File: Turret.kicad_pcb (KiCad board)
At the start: 2 copper layers, 104 x 54 mm, 26 parts, among them J1 172298-1108, J2 501645-1620

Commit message: Cleaned up hiearchical labels and local labels
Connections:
- net /SWD_3V3 renamed /SWD_{3V3}
- net /SWD_GND renamed /SWD_{GND}
- net /SWD_SWCLK renamed /SWD_{SWCLK}
- net /SWD_SWDIO renamed /SWD_{SWDIO}

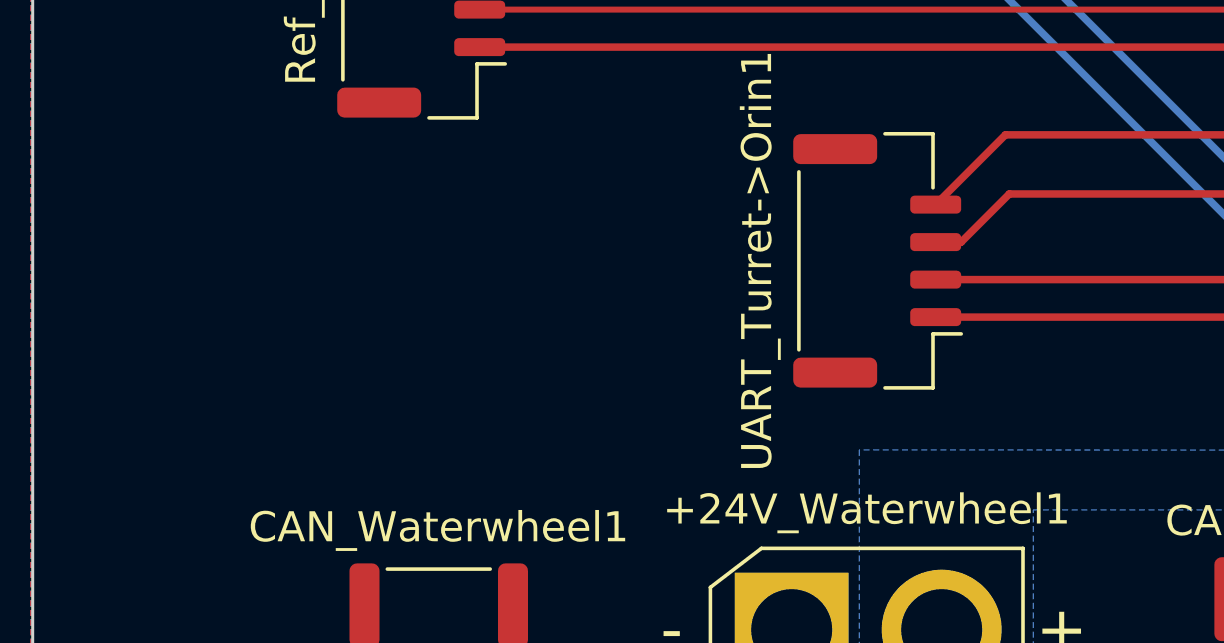
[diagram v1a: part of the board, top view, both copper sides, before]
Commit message: Added UV LED connection
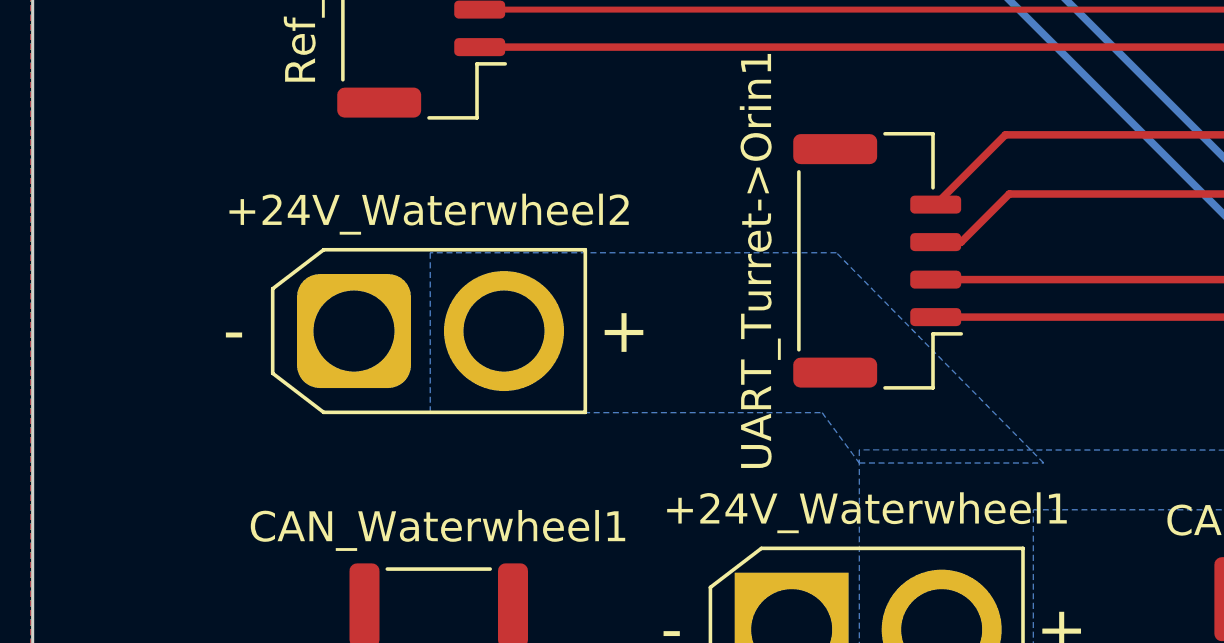
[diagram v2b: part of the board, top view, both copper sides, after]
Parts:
- added +24V_Waterwheel2: Conn_01x02_Pin, Connector_AMASS:AMASS_XT30U-F_1x02_P5.0mm_Vertical, F.Cu at (51.2, 69.0)
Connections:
- net /+19V renamed /OrinPWR_{+19V}
- net /+24V_Gimbal renamed /Gimbal_{+24V}
- net /+24V_Shooter renamed /Shooter_{+24V}
- net /CANGim_H renamed /CAN1+
- net /CANGim_L renamed /CAN1-
- net /CANH renamed /CAN2+
- net /CANL renamed /CAN2-
- net /Gimbal_PWR_GND renamed /Gimbal_{GND}
- net /Orin_PWR_GND renamed /OrinPWR_{GND}
- net /Ref_CAN+ renamed /Ref_{CAN}+
- net /Ref_CAN- renamed /Ref_{CAN}-
- net /Ref_GND renamed /Ref_{GND}
- net /Ref_PWR renamed /Ref_{PWR}
- net /Shooter_PWR_GND renamed /Shooter_{GND}
- net /UART_3V3 renamed /UART_{3V3}
- net /UART_GND renamed /UART_{GND}
- net /UART_RX renamed /UART_{RX}
- net /UART_TX renamed /UART_{TX}
